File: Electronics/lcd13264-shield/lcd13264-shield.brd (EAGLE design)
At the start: 96.5 x 54.6 mm, 56 parts, among them J1 MICRO-SDCARD-CONNECTOR-330006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, J3 ARDUINO_R3_SHIELDUNO_R3_SHIEL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, Q1 PNP-500mA, X1 FH12-12S-1S, X2 FH12-12S-1S

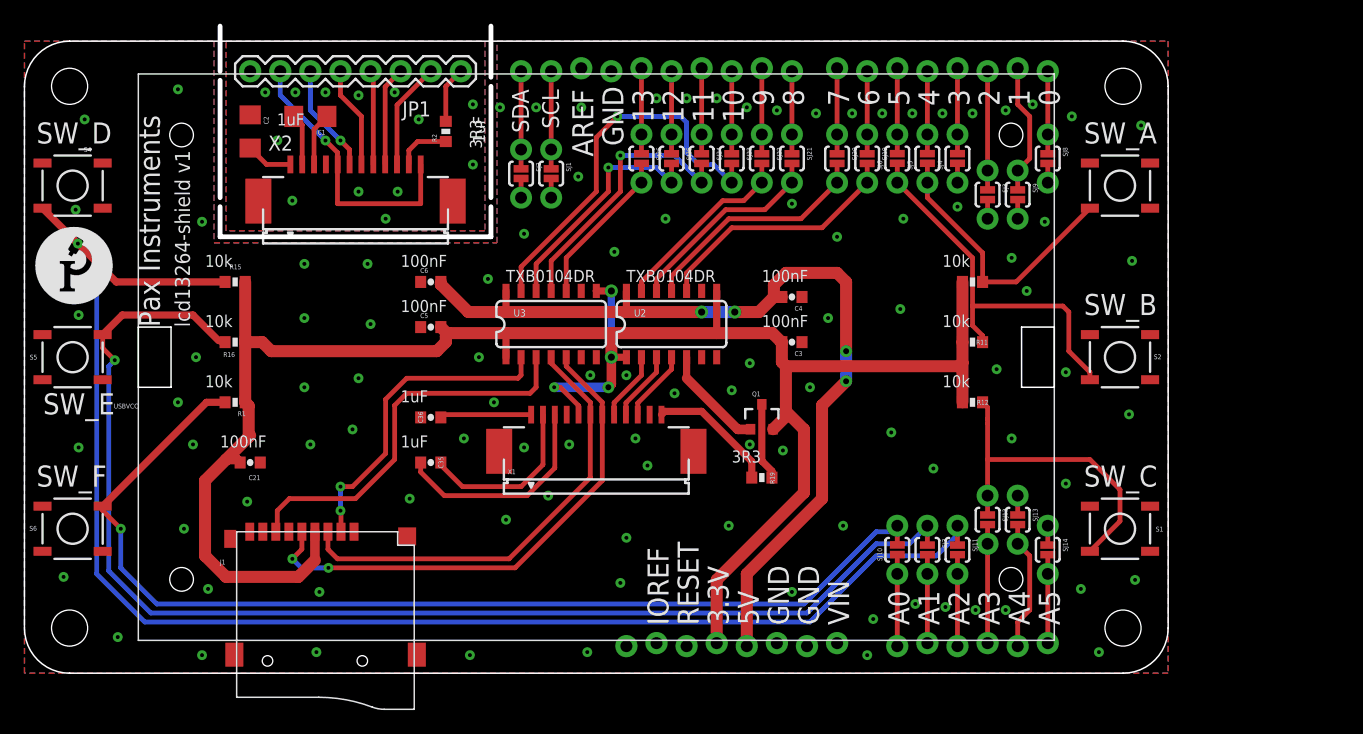
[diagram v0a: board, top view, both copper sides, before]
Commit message: Closed all the silkscreen issues.
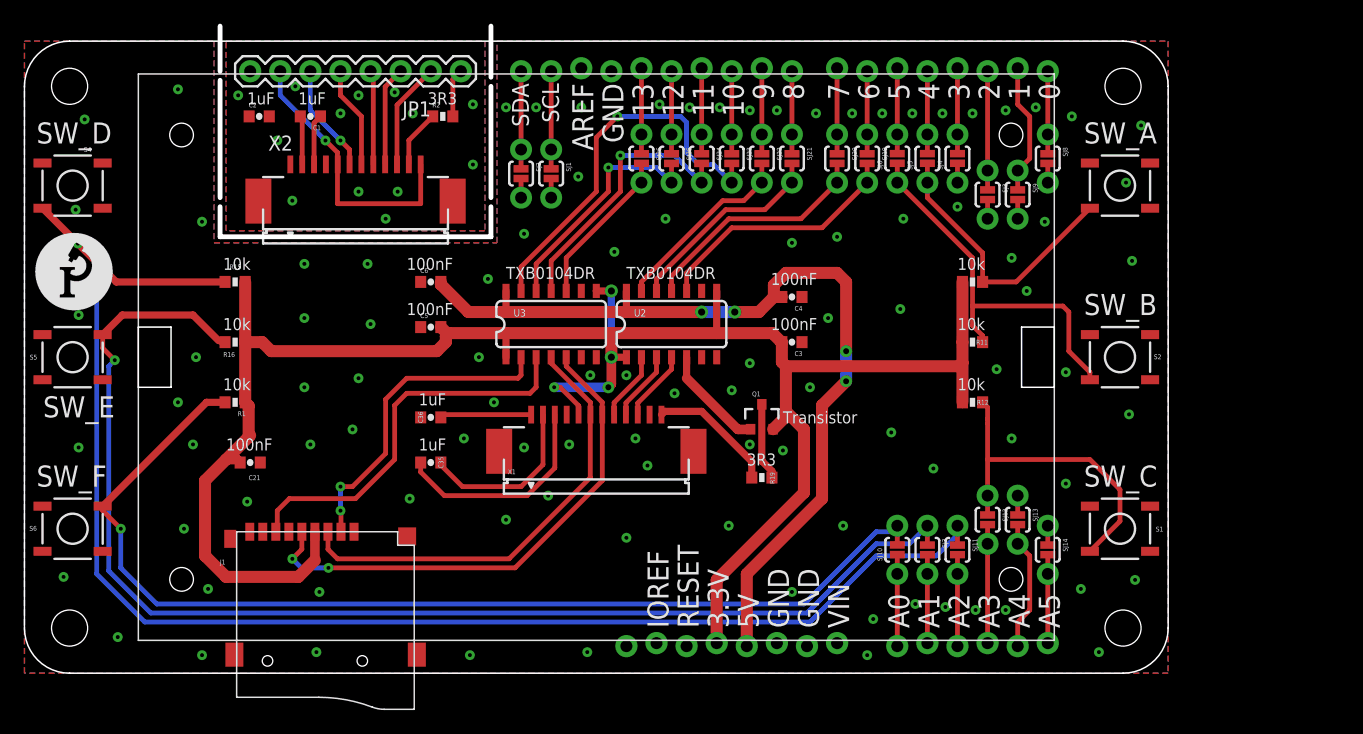
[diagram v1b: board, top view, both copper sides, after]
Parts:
- C1, C2: device PaxInstrument-T400:SPARKFUN-CAPACITORS_1206 -> PaxInstrument-T400:SPARKFUN-CAPACITORS_0603-CAP
- moved U$6 61.2 mm to (95.2, 47.0), turned to 270 degrees
- moved C2 1.48 mm to (19.8, 47.0), turned to 0 degrees
- moved R2 1.30 mm to (35.3, 47.0), turned to 0 degrees
- moved U$1 0.51 mm to (0.76, 30.5)
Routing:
- net N$42: track 3.96 -> 0.00 mm
- net N$51: track 4.76 -> 4.09 mm
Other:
- board text added: "Arduino SD_CS 10 SW_A 4 SW_B 5 SW_C A3 SW_D A2 SW_E A1 SW_F A0 MOSI 11 MISO 12 SCK 13 LCD_A0 9 LCD_RST 8 LCD_CS 7 LCD_BL 6"
- board text added: "LCD_A0"
- board text added: "LCD_BL"
- board text added: "LCD_CS"
- board text added: "LCD_RST"
- board text added: "MOSI"
- board text added: "SCK"
- board text added: "Transistor"
- board text removed: "Pin Map SD_CS 10 SW_A 4 SW_B 5 SW_C A3 SW_D A2 SW_E A1 SW_F A0 MOSI 11 MISO 12 SCK 13 LCD_A0 9 LCD_RST 8 LCD_CS 7 LCD_BL 6"

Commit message: Added pin function labels to top and bottom. Verified silkscreen.
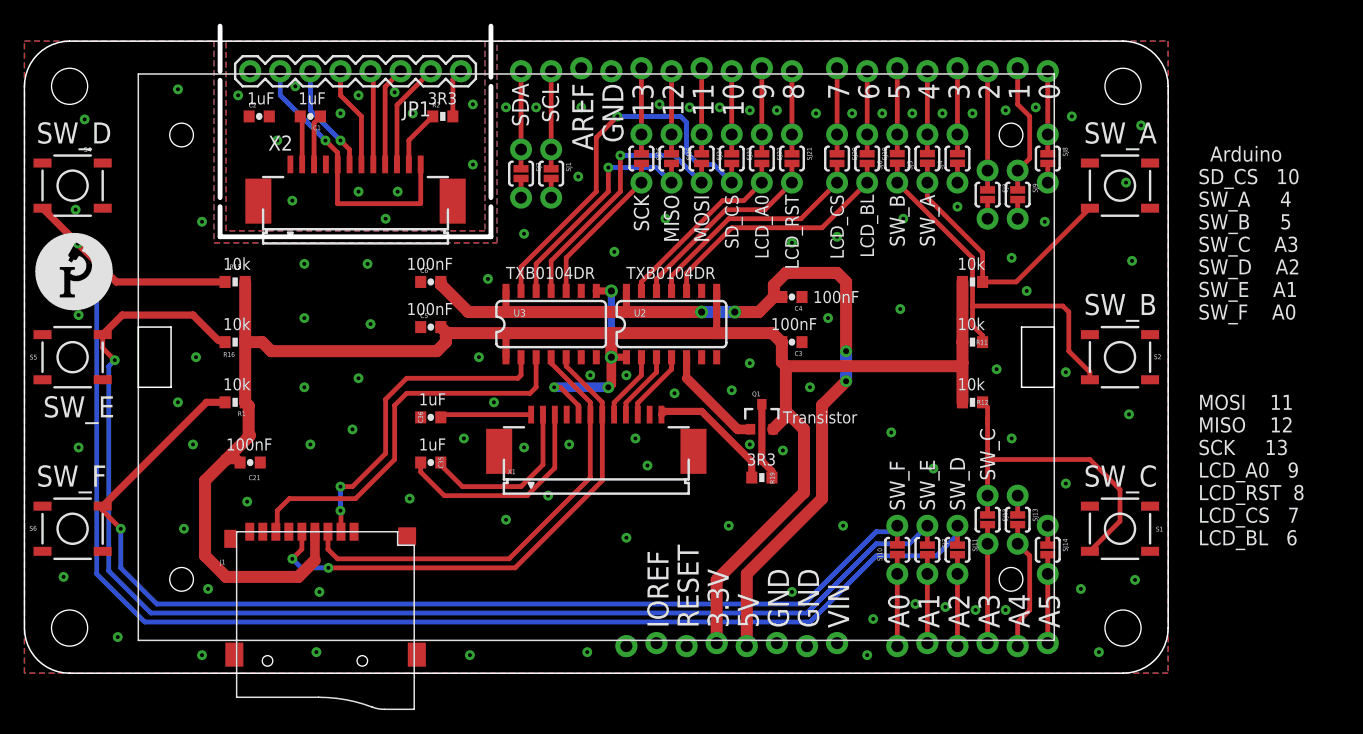
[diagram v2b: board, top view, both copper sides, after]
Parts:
- moved U$6 41.1 mm to (88.9, 6.35), turned to 90 degrees
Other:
- board text added: "MISO"
- board text added: "SD_CS"
- board text added: "lcd13264-shield v3"
- board text added: "paxinstruments.com/products/sku1003"
- board text removed: "lcd13264-shield v1"
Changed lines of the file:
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@@
 <layer number="17" name="Pads" color="2" fill="1" visible="yes" active="yes"/>
 <layer number="18" name="Vias" color="2" fill="1" visible="yes" active="yes"/>
-<layer number="19" name="Unrouted" color="6" fill="1" visible="no" active="yes"/>
+<layer number="19" name="Unrouted" color="6" fill="1" visible="yes" active="yes"/>
 <layer number="20" name="Dimension" color="13" fill="1" visible="yes" active="yes"/>
 <layer number="21" name="tPlace" color="7" fill="1" visible="yes" active="yes"/>
@@
 <layer number="31" name="tCream" color="7" fill="4" visible="yes" active="yes"/>
 <layer number="32" name="bCream" color="7" fill="5" visible="yes" active="yes"/>
-<layer number="33" name="tFinish" color="6" fill="3" visible="yes" active="yes"/>
-<layer number="34" name="bFinish" color="6" fill="6" visible="yes" active="yes"/>
-<layer number="35" name="tGlue" color="7" fill="4" visible="yes" active="yes"/>
-<layer number="36" name="bGlue" color="7" fill="5" visible="yes" active="yes"/>
+<layer number="33" name="tFinish" color="6" fill="3" visible="no" active="yes"/>
+<layer number="34" name="bFinish" color="6" fill="6" visible="no" active="yes"/>
+<layer number="35" name="tGlue" color="7" fill="4" visible="no" active="yes"/>
+<layer number="36" name="bGlue" color="7" fill="5" visible="no" active="yes"/>
 <layer number="37" name="tTest" color="7" fill="1" visible="no" active="yes"/>
 <layer number="38" name="bTest" color="7" fill="1" visible="no" active="yes"/>
-<layer number="39" name="tKeepout" color="4" fill="11" visible="yes" active="yes"/>
-<layer number="40" name="bKeepout" color="1" fill="11" visible="yes" active="yes"/>
-<layer number="41" name="tRestrict" color="4" fill="10" visible="yes" active="yes"/>
-<layer number="42" name="bRestrict" color="1" fill="10" visible="yes" active="yes"/>
-<layer number="43" name="vRestrict" color="2" fill="10" visible="yes" active="yes"/>
+<layer number="39" name="tKeepout" color="4" fill="11" visible="no" active="yes"/>
+<layer number="40" name="bKeepout" color="1" fill="11" visible="no" active="yes"/>
+<layer number="41" name="tRestrict" color="4" fill="10" visible="no" active="yes"/>
+<layer number="42" name="bRestrict" color="1" fill="10" visible="no" active="yes"/>
+<layer number="43" name="vRestrict" color="2" fill="10" visible="no" active="yes"/>
 <layer number="44" name="Drills" color="7" fill="1" visible="no" active="yes"/>
-<layer number="45" name="Holes" color="7" fill="1" visible="yes" active="yes"/>
-<layer number="46" name="Milling" color="3" fill="1" visible="yes" active="yes"/>
+<layer number="45" name="Holes" color="7" fill="1" visible="no" active="yes"/>
+<layer number="46" name="Milling" color="3" fill="1" visible="no" active="yes"/>
 <layer number="47" name="Measures" color="7" fill="1" visible="no" active="yes"/>
-<layer number="48" name="Document" color="7" fill="1" visible="yes" active="yes"/>
-<layer number="49" name="Reference" color="7" fill="1" visible="yes" active="yes"/>
+<layer number="48" name="Document" color="7" fill="1" visible="no" active="yes"/>
+<layer number="49" name="Reference" color="7" fill="1" visible="no" active="yes"/>
 <layer number="50" name="dxf" color="7" fill="1" visible="no" active="no"/>
-<layer number="51" name="tDocu" color="6" fill="1" visible="yes" active="yes"/>
-<layer number="52" name="bDocu" color="7" fill="1" visible="yes" active="yes"/>
+<layer number="51" name="tDocu" color="6" fill="1" visible="no" active="yes"/>
+<layer number="52" name="bDocu" color="7" fill="1" visible="no" active="yes"/>
 <layer number="53" name="tGND_GNDA" color="7" fill="9" visible="no" active="no"/>
 <layer number="54" name="bGND_GNDA" color="1" fill="9" visible="no" active="no"/>
@@
 <text x="72.898" y="49.784" size="1.778" layer="21" rot="R270">5</text>
 <text x="75.438" y="49.784" size="1.778" layer="21" rot="R270">4</text>
-<text x="94.996" y="39.37" size="1.6764" layer="22" rot="MR270">lcd13264-shield v1</text>
-<text x="92.71" y="39.37" size="2.54" layer="22" rot="MR270">Pax Instruments</text>
+<text x="90.424" y="13.97" size="1.6764" layer="22" rot="MR90">lcd13264-shield v3</text>
+<text x="92.71" y="13.97" size="2.54" layer="22" rot="MR90">Pax Instruments</text>
 <text x="16.764" y="23.876" size="1.016" layer="21">10k</text>
 <text x="16.764" y="28.956" size="1.016" layer="21">10k</text>
@@
 <text x="32.258" y="34.036" size="1.016" layer="21">100nF</text>
 <text x="62.992" y="28.956" size="1.016" layer="21">100nF</text>
-<text x="62.992" y="32.766" size="1.016" layer="21">100nF</text>
+<text x="66.548" y="31.242" size="1.016" layer="21">100nF</text>
 <hole x="3.81" y="49.53" drill="3.048"/>
 <hole x="92.71" y="49.53" drill="3.048"/>
@@
 <wire x1="86.868" y1="10.16" x2="86.36" y2="10.16" width="0.3048" layer="22"/>
 <wire x1="86.36" y1="10.16" x2="86.36" y2="9.652" width="0.3048" layer="22"/>
+<text x="88.392" y="13.97" size="1.27" layer="22" rot="MR90">paxinstruments.com/products/sku1003</text>
+<text x="99.06" y="44.45" size="1.27" layer="21" font="vector" ratio="15" align="top-left">  Arduino
+SD_CS   10
+SW_A     4
+SW_B     5
+SW_C    A3
+SW_D    A2
+SW_E    A1
+SW_F    A0
+MOSI    11
+MISO    12
+SCK     13
+LCD_A0   9
+LCD_RST  8
+LCD_CS   7
+LCD_BL   6</text>
+<text x="59.69" y="40.386" size="1.143" layer="21" rot="R270" align="center-left">SD_CS</text>
+<text x="76.2" y="40.386" size="1.27" layer="21" rot="R270" align="center-left">SW_A</text>
+<text x="73.66" y="40.386" size="1.27" layer="21" rot="R270" align="center-left">SW_B</text>
+<text x="81.28" y="16.256" size="1.27" layer="21" rot="R90" align="center-left">SW_C</text>
+<text x="78.74" y="13.716" size="1.27" layer="21" rot="R90" align="center-left">SW_D</text>
+<text x="76.2" y="13.716" size="1.27" layer="21" rot="R90" align="center-left">SW_E</text>
+<text x="73.66" y="13.716" size="1.27" layer="21" rot="R90" align="center-left">SW_F</text>
+<text x="57.15" y="40.386" size="1.27" layer="21" rot="R270" align="center-left">MOSI</text>
+<text x="54.61" y="40.386" size="1.27" layer="21" rot="R270" align="center-left">MISO</text>
+<text x="52.07" y="40.386" size="1.27" layer="21" rot="R270" align="center-left">SCK</text>
+<text x="62.23" y="40.386" size="1.143" layer="21" rot="R270" align="center-left">LCD_A0</text>
+<text x="64.77" y="40.386" size="1.143" layer="21" rot="R270" align="center-left">LCD_RST</text>
+<text x="68.58" y="40.386" size="1.143" layer="21" rot="R270" align="center-left">LCD_CS</text>
+<text x="71.12" y="40.386" size="1.143" layer="21" rot="R270" align="center-left">LCD_BL</text>
+<text x="52.07" y="40.386" size="1.27" layer="22" rot="MR270" align="center-left">SCK</text>
+<text x="54.61" y="40.386" size="1.27" layer="22" rot="MR270" align="center-left">MISO</text>
+<text x="57.15" y="40.386" size="1.27" layer="22" rot="MR270" align="center-left">MOSI</text>
+<text x="59.69" y="40.386" size="1.143" layer="22" rot="MR270" align="center-left">SD_CS</text>
+<text x="62.23" y="40.386" size="1.143" layer="22" rot="MR270" align="center-left">LCD_A0</text>
+<text x="64.77" y="40.386" size="1.143" layer="22" rot="MR270" align="center-left">LCD_RST</text>
+<text x="68.58" y="40.386" size="1.143" layer="22" rot="MR270" align="center-left">LCD_CS</text>
+<text x="71.12" y="40.386" size="1.143" layer="22" rot="MR270" align="center-left">LCD_BL</text>
+<text x="73.66" y="40.386" size="1.27" layer="22" rot="MR270" align="center-left">SW_B</text>
+<text x="76.2" y="40.386" size="1.27" layer="22" rot="MR270" align="center-left">SW_A</text>
+<text x="73.66" y="13.716" size="1.27" layer="22" rot="MR90" align="center-left">SW_F</text>
+<text x="76.2" y="13.716" size="1.27" layer="22" rot="MR90" align="center-left">SW_E</text>
+<text x="78.74" y="13.716" size="1.27" layer="22" rot="MR90" align="center-left">SW_D</text>
+<text x="81.28" y="16.256" size="1.27" layer="22" rot="MR90" align="center-left">SW_C</text>
 </plain>
 <attributes>
@@
 <attribute name="VALUE" x="20.574" y="15.621" size="0.4064" layer="27" font="vector" rot="R180"/>
 </element>
-<element name="U$6" library="PaxInstrument-T400" package="PAXINSTRUMENT_LOGO" value="" x="95.25" y="46.99" rot="MR270"/>
+<element name="U$6" library="PaxInstrument-T400" package="PAXINSTRUMENT_LOGO" value="" x="88.9" y="6.35" rot="MR90"/>
 <element name="R1" library="PaxInstrument-T400" package="SPARKFUN-RESISTORS_0603-RES" value="10k" x="17.78" y="22.86" rot="R180">
 <attribute name="MPN" value="RC1608J103CS" x="17.78" y="22.86" size="1.778" layer="27" rot="R180" display="off"/>
